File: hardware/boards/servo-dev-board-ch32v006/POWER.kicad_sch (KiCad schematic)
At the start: 16 parts, among them J1 JST-PH-H, J2 TERM, U1 HT7533-1

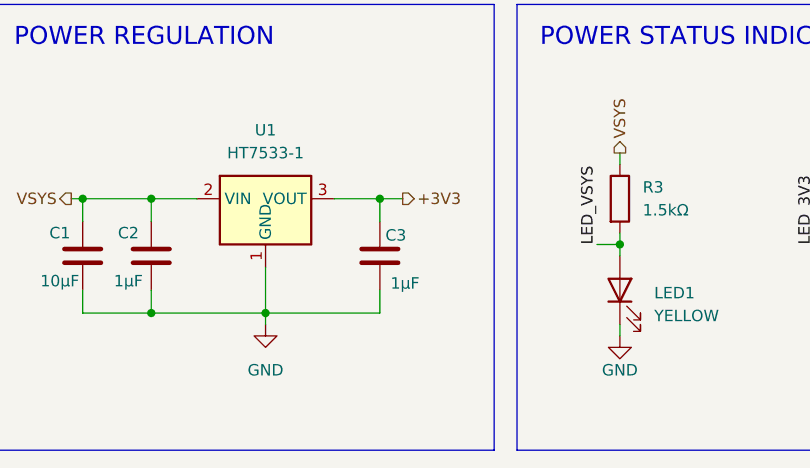
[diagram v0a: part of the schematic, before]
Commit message: fix LDO output caps
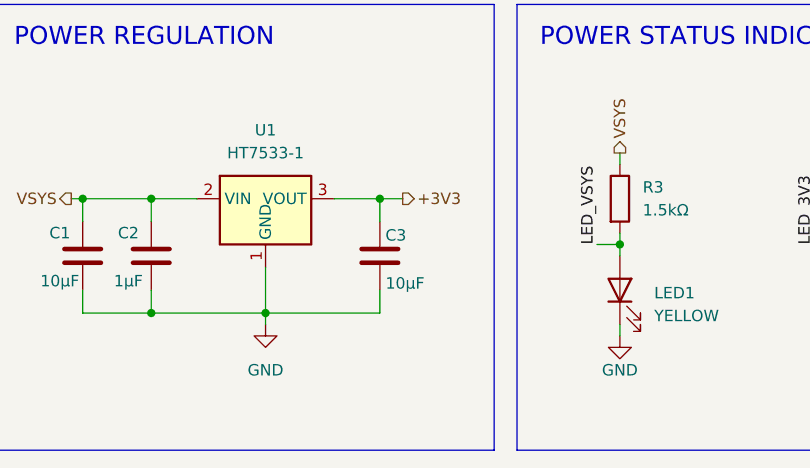
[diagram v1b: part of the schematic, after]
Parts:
- C3: value 1µF -> 10µF
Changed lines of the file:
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@@
 			)
 		)
-		(property "Value" "1µF"
+		(property "Value" "10µF"
 			(at 108.204 110.998 0)
 			(effects

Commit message: updated LCSC part numbers for all symbols
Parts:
- C1: LCSC C96446 -> C440198
- C2: LCSC C52923 -> C28323
- C3: LCSC C52923 -> C440198
- J2: LCSC (none) -> C8465
- R1, R2: LCSC C25905 -> C27834
- R3: LCSC C25879 -> C4310
- R4: LCSC C25104 -> C17710
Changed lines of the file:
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@@
 			)
 		)
-		(property "LCSC" "C52923"
+		(property "LCSC" "C28323"
 			(at 77.47 105.41 0)
 			(effects
@@
 			)
 		)
-		(property "LCSC" "C25879"
+		(property "LCSC" "C4310"
 			(at 134.62 100.3299 0)
 			(effects
@@
 			)
 		)
+		(property "LCSC" "C8465"
+			(at 157.48 48.26 0)
+			(effects
+				(font
+					(size 1.27 1.27)
+				)
+				(hide yes)
+			)
+		)
 		(pin "1"
 		)
@@
 			)
 		)
-		(property "LCSC" "C25905"
+		(property "LCSC" "C27834"
 			(at 80.518 42.926 0)
 			(effects
@@
 			)
 		)
-		(property "LCSC" "C25905"
+		(property "LCSC" "C27834"
 			(at 80.518 51.816 0)
 			(effects
@@
 			)
 		)
-		(property "LCSC" "C96446"
+		(property "LCSC" "C440198"
 			(at 69.85 105.41 0)
 			(effects
@@
 			)
 		)
-		(property "LCSC" "C52923"
+		(property "LCSC" "C440198"
 			(at 107.188 105.664 0)
 			(effects
@@
 			)
 		)
-		(property "LCSC" "C25104"
+		(property "LCSC" "C17710"
 			(at 158.75 100.3299 0)
 			(effects

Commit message: remove 'LCSC Part' Property from project
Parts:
- J1: LCSC Part C173752 -> (none)
- J2: LCSC Part C8465 -> (none)
- USB1: LCSC Part C668623 -> (none)
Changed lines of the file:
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@@
-			)
-		)
-		(property "LCSC Part" "C8465"
-			(at 157.48 68.58 0)
-			(effects
-				(font
-					(size 1.27 1.27)
-				)
-				(hide yes)
 			)
 		)
@@
 		(property "Description" "Generic connector, single row, 01x02, script generated (kicad-library-utils/schlib/autogen/connector/)"
 			(at 115.57 50.8 0)
-			(effects
-				(font
-					(size 1.27 1.27)
-				)
-				(hide yes)
-			)
-		)
-		(property "LCSC Part" "C173752"
-			(at 115.57 64.77 0)
 			(effects
 				(font
@@
 			(effects
 				(font
-					(size 1.27 1.27)
-				)
-				(hide yes)
-			)
-		)
-		(property "LCSC Part" "C668623"
-			(at 33.02 71.12 0)
-			(effects
-				(font

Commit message: added MFPN properties
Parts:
- C1, C3: MFPN (none) -> GRM21BR61H106KE43L
- C2: MFPN (none) -> CL21B105KBFNNNE
- D1, D2, D3: MFPN (none) -> SS54
- J1: MFPN (none) -> S2B-PH-K-S(LF)(SN)
- J2: MFPN (none) -> WJ500V-5.08-2P
- LED1: MFPN (none) -> KT-0805Y
- LED2: MFPN (none) -> KT-0805G
- R1, R2: MFPN (none) -> 0805W8F5101T5E
- R3: MFPN (none) -> 0805W8F1501T5E
- R4: MFPN (none) -> 0805W8F4700T5E
- U1: MFPN (none) -> HT7533-1
- USB1: MFPN (none) -> TYPE-C 6P(073)
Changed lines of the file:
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@@
+			)
+		)
+		(property "MFPN" "CL21B105KBFNNNE"
+			(at 77.47 105.41 0)
+			(effects
+				(font
+					(size 1.27 1.27)
+				)
+				(hide yes)
 			)
 		)
@@
 			)
 		)
+		(property "MFPN" "KT-0805Y"
+			(at 135.89 112.0774 0)
+			(effects
+				(font
+					(size 1.27 1.27)
+				)
+				(hide yes)
+			)
+		)
 		(property "Sim.Pins" "1=K 2=A"
 			(at 132.08 111.76 0)
@@
 			)
 		)
+		(property "MFPN" "0805W8F1501T5E"
+			(at 134.62 100.3299 0)
+			(effects
+				(font
+					(size 1.27 1.27)
+				)
+				(hide yes)
+			)
+		)
 		(pin "1"
 		)
@@
 			)
 		)
+		(property "MFPN" "WJ500V-5.08-2P"
+			(at 157.48 48.26 0)
+			(effects
+				(font
+					(size 1.27 1.27)
+				)
+				(hide yes)
+			)
+		)
 		(pin "1"
 		)
@@
 			)
 		)
+		(property "MFPN" "0805W8F5101T5E"
+			(at 80.518 42.926 0)
+			(effects
+				(font
+					(size 1.27 1.27)
+				)
+				(hide yes)
+			)
+		)
 		(pin "1"
 		)
@@
 			)
 		)
+		(property "MFPN" "HT7533-1"
+			(at 92.71 104.14 0)
+			(effects
+				(font
+					(size 1.27 1.27)
+				)
+				(hide yes)
+			)
+		)
 		(property "JLC Type" "Basic"
 			(at 92.71 104.14 0)
@@
 			)
 		)
+		(property "MFPN" "0805W8F5101T5E"
+			(at 80.518 51.816 0)
+			(effects
+				(font
+					(size 1.27 1.27)
+				)
+				(hide yes)
+			)
+		)
 		(pin "1"
 		)
@@
 			)
 		)
+		(property "MFPN" "SS54"
+			(at 34.29 93.98 0)
+			(effects
+				(font
+					(size 1.27 1.27)
+				)
+				(hide yes)
+			)
+		)
 		(property "JLC Type" "Basic"
 			(at 34.29 93.98 0)
@@
 			)
 		)
+		(property "MFPN" "S2B-PH-K-S(LF)(SN)"
+			(at 116.84 41.91 0)
+			(effects
+				(font
+					(size 1.27 1.27)
+				)
+				(hide yes)
+			)
+		)
 		(property "JLC Type" "Extended"
 			(at 115.57 50.8 0)
@@
 		)
 		(property "LCSC" "C22452"
+			(at 34.29 114.3 0)
+			(effects
+				(font
+					(size 1.27 1.27)
+				)
+				(hide yes)
+			)
+		)
+		(property "MFPN" "SS54"
 			(at 34.29 114.3 0)
 			(effects
@@
 			)
 		)
+		(property "MFPN" "TYPE-C 6P(073)"
+			(at 33.02 38.1 0)
+			(effects
+				(font
+					(size 1.27 1.27)
+				)
+				(hide yes)
+			)
+		)
 		(property "JLC Type" "Extended"
 			(at 33.02 50.8 0)
@@
 			)
 		)
+		(property "MFPN" "SS54"
+			(at 34.29 104.14 0)
+			(effects
+				(font
+					(size 1.27 1.27)
+				)
+				(hide yes)
+			)
+		)
 		(property "JLC Type" "Basic"
 			(at 34.29 104.14 0)
@@
 			)
 		)
+		(property "MFPN" "GRM21BR61H106KE43L"
+			(at 69.85 105.41 0)
+			(effects
+				(font
+					(size 1.27 1.27)
+				)
+				(hide yes)
+			)
+		)
 		(pin "1"
 		)
@@
 		)
 		(property "LCSC" "C440198"
+			(at 107.188 105.664 0)
+			(effects
+				(font
+					(size 1.27 1.27)
+				)
+				(hide yes)
+			)
+		)
+		(property "MFPN" "GRM21BR61H106KE43L"
 			(at 107.188 105.664 0)
 			(effects
@@
 			)
 		)
+		(property "MFPN" "KT-0805G"
+			(at 160.02 112.0774 0)
+			(effects
+				(font
+					(size 1.27 1.27)
+				)
+				(hide yes)
+			)
+		)
 		(property "Sim.Pins" "1=K 2=A"
 			(at 156.21 111.76 0)
@@
 			(at 158.75 100.3299 0)
 			(effects
+				(font
+					(size 1.27 1.27)
+				)
+				(hide yes)
+			)
+		)
+		(property "MFPN" "0805W8F4700T5E"
+			(at 158.75 100.3299 0)
+			(effects

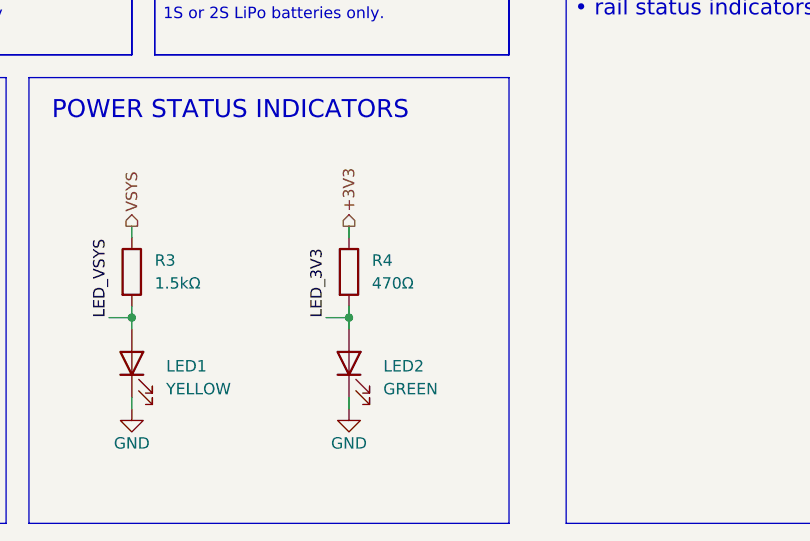
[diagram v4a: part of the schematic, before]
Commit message: Revision V1B. Fixes:
* Fixed reversed VDD/VCC on MCU.
* Fixed TP silk screen labels on top row.
* Updated RS1 to 10mOhm/333mW.
* Updated System (green) LED resistor to 1.5kOhm to reduce brightness.
* Aligned bottom row TPs to center of board.
* Updated text on back silkscreen to reflect version / RS1 updates.
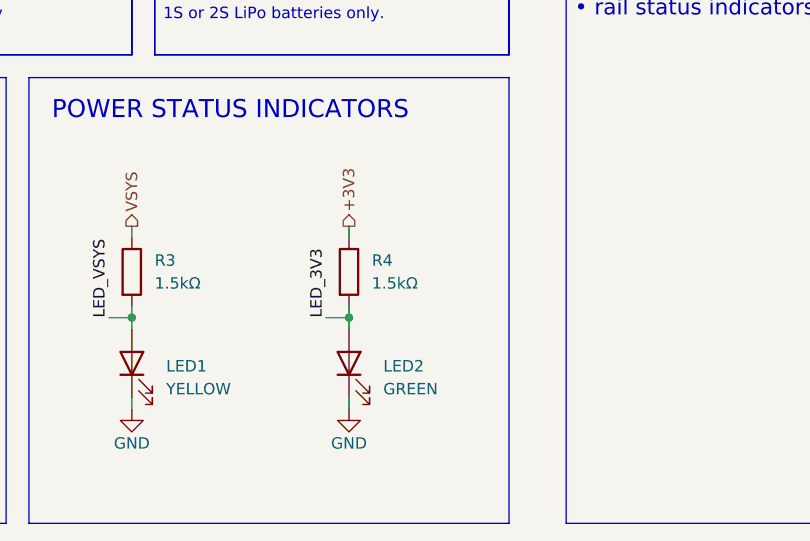
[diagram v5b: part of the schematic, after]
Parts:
- R4: value 470Ω -> 1.5kΩ; LCSC C17710 -> C4310; MFPN 0805W8F4700T5E -> 0805W8F1501T5E

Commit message: update board
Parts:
- added D4: SS54, Diode_SMD:D_SMA_Handsoldering, symbol Diode:SS34
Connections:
- net GND: now also J1.1 (Pin_1); no longer J1.2 (Pin_2)
- net VBAT: now also J1.2 (Pin_2); no longer J1.1 (Pin_1)
- net VSYS: now also D4.1 (K)
- new net VPROG: D4.2 (A)
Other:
- moved on the sheet: D1, D2, D3, J1
